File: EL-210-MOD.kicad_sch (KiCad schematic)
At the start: 29 parts, among them J1 Conn_01x05, J2 Conn_01x02, P1 EL-210-KEY, U1 9-ST-20, U2 STM32G0B1KET6, U3 MAX6934AQH+D, U4 TPS613221ADBV, U5 MAX4719EUB+, U6 TLV61046ADB

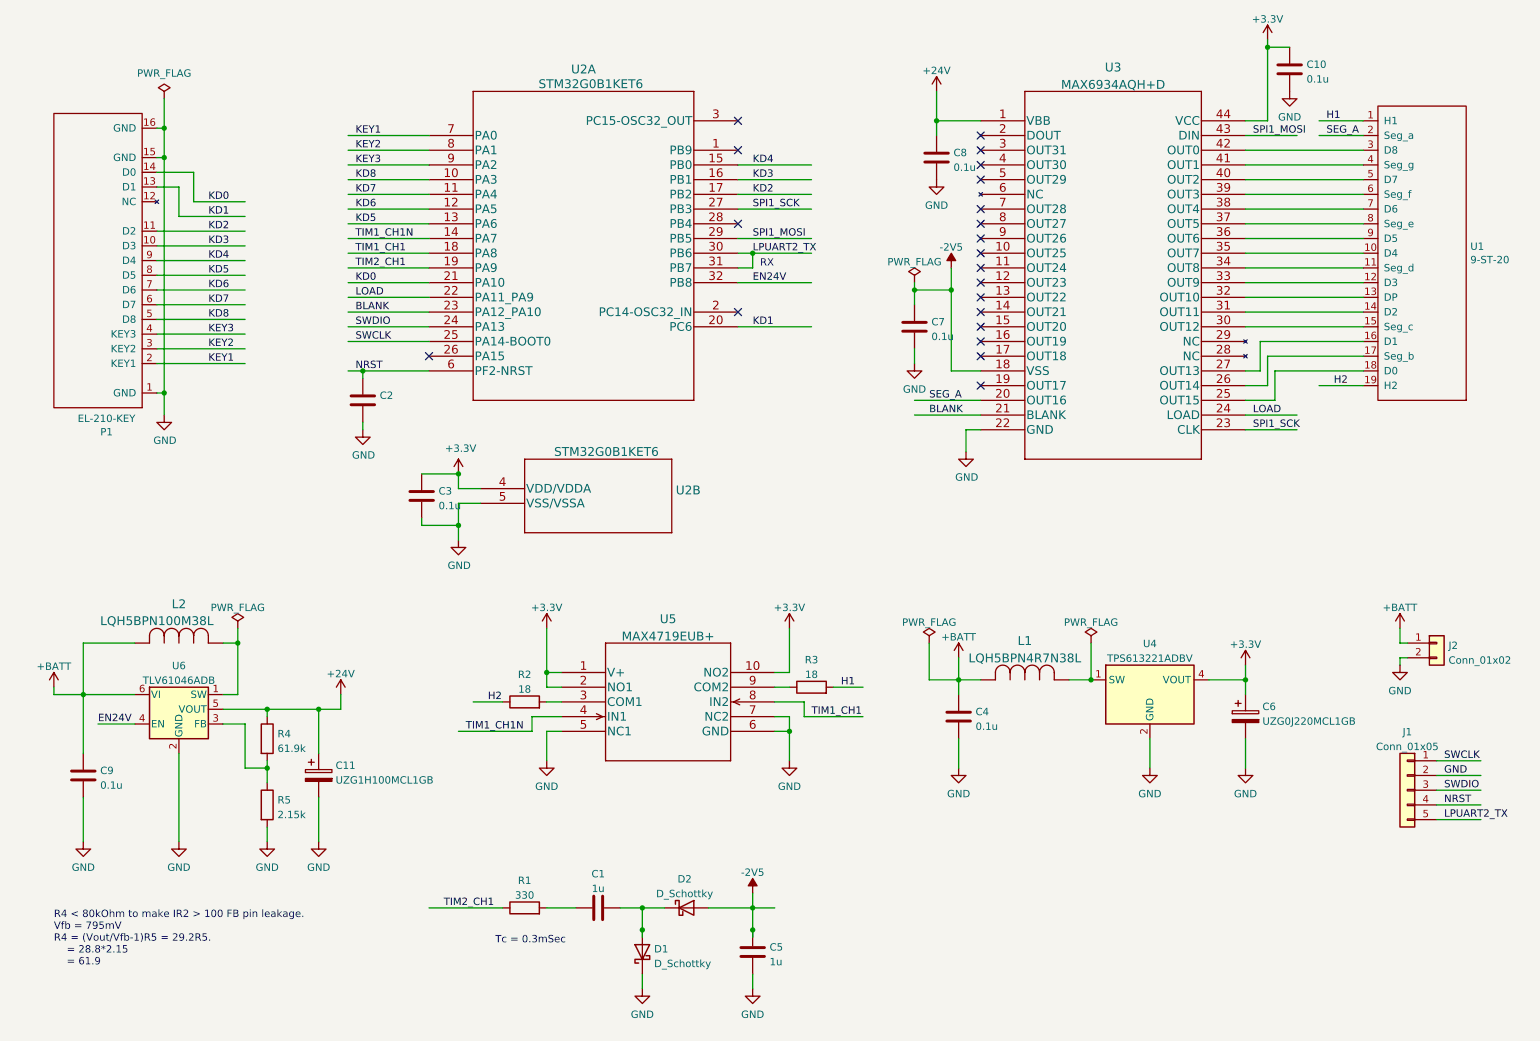
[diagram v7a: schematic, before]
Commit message: Layout finished.
DRC passed except silkscreen minor problem.
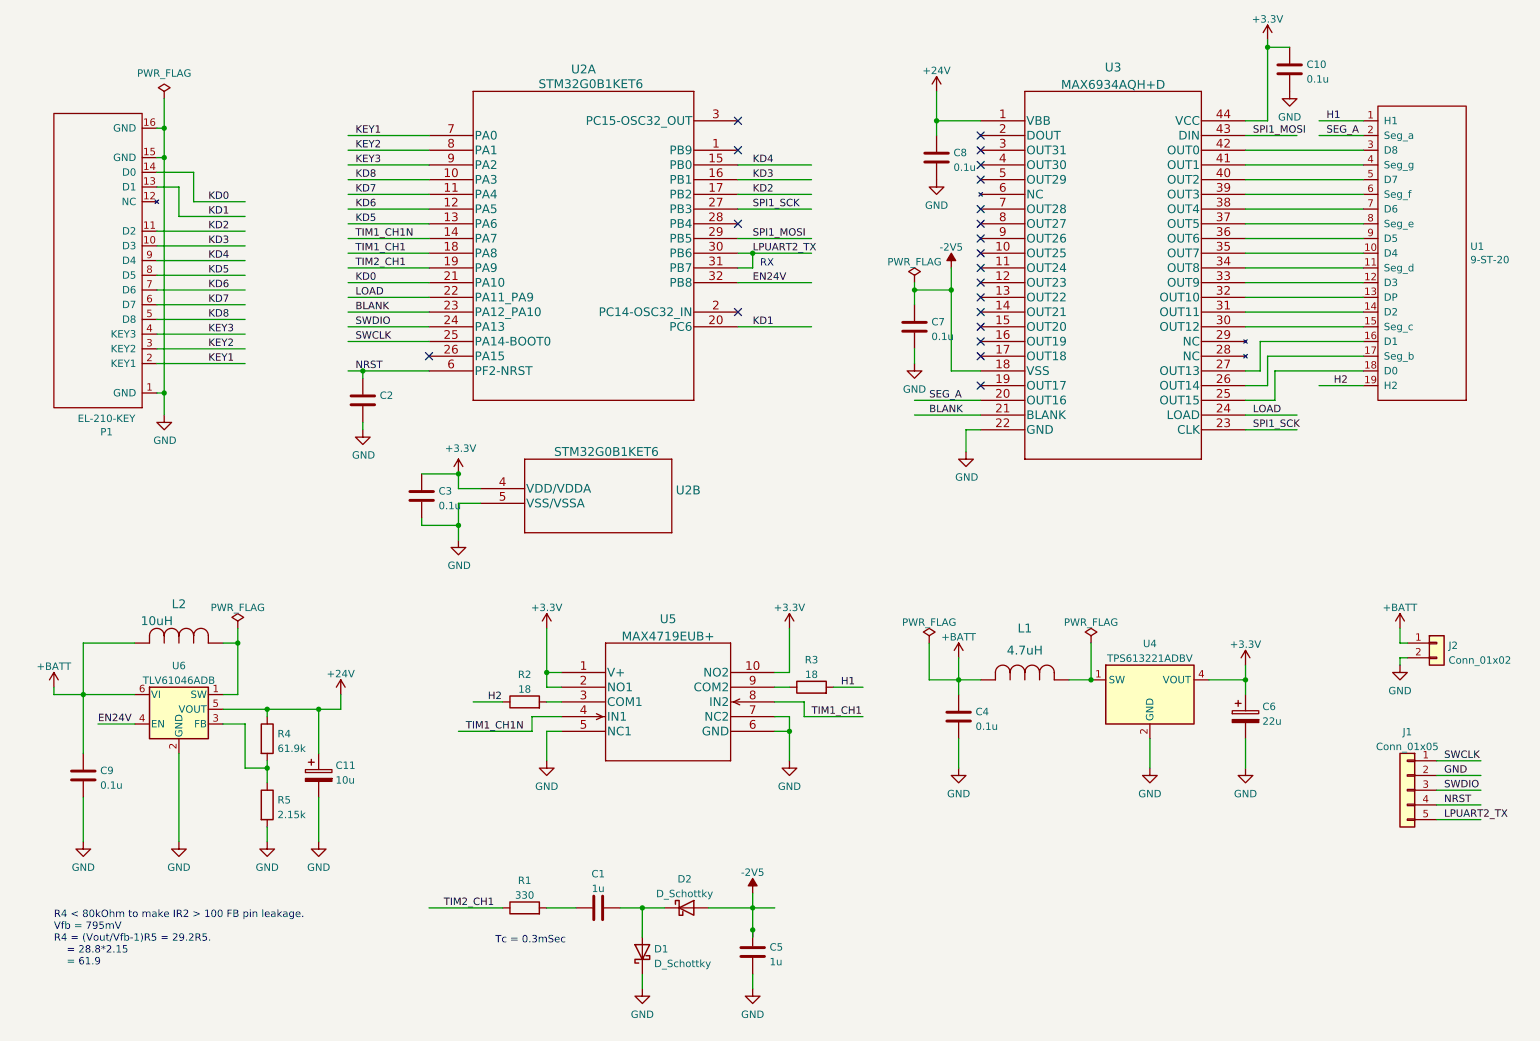
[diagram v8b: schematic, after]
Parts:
- C11: value UZG1H100MCL1GB -> 10u
- C6: value UZG0J220MCL1GB -> 22u
- L1: value LQH5BPN4R7N38L -> 4.7uH
- L2: value LQH5BPN100M38L -> 10uH
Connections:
- net at C1.2, D2.1 (K): no longer D1.2 (A)
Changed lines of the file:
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@@
   (junction (at 148.59 58.42) (diameter 0) (color 0 0 0 0)
-  )
-  (junction (at 129.54 175.26) (diameter 0) (color 0 0 0 0)
   )
   (junction (at 46.99 36.83) (diameter 0) (color 0 0 0 0)
@@
     (stroke (width 0) (type default) (color 0 0 0 0))
   )
-  (wire (pts (xy 129.54 171.45) (xy 129.54 175.26))
-    (stroke (width 0) (type default) (color 0 0 0 0))
-  )
   (wire (pts (xy 140.97 171.45) (xy 148.59 171.45))
     (stroke (width 0) (type default) (color 0 0 0 0))
@@
     (stroke (width 0) (type default) (color 0 0 0 0))
   )
-  (wire (pts (xy 129.54 175.26) (xy 129.54 176.53))
+  (wire (pts (xy 129.54 171.45) (xy 129.54 176.53))
     (stroke (width 0) (type default) (color 0 0 0 0))
   )
@@
       (effects (font (size 1.27 1.27)) hide)
     )
-    (property "Datasheet" "~" (id 3) (at 184.15 138.43 0)
+    (property "Datasheet" "1608M" (id 3) (at 184.15 138.43 0)
       (effects (font (size 1.27 1.27)) hide)
     )
@@
       (effects (font (size 1.27 1.27)) hide)
     )
-    (property "Datasheet" "~" (id 3) (at 121.92 171.45 0)
+    (property "Datasheet" "1608M" (id 3) (at 121.92 171.45 0)
       (effects (font (size 1.27 1.27)) hide)
     )
@@
       (effects (font (size 1.27 1.27)) hide)
     )
-    (property "Datasheet" "~" (id 3) (at 64.77 153.67 0)
+    (property "Datasheet" "1608M" (id 3) (at 64.77 153.67 0)
       (effects (font (size 1.27 1.27)) hide)
     )
@@
       (effects (font (size 1.27 1.27)) hide)
     )
-    (property "Datasheet" "~" (id 3) (at 109.22 171.45 0)
+    (property "Datasheet" "1608M" (id 3) (at 109.22 171.45 0)
       (effects (font (size 1.27 1.27)) hide)
     )
@@
       (effects (font (size 1.27 1.27)) (justify left))
     )
-    (property "Value" "UZG1H100MCL1GB" (id 1) (at 76.581 149.4032 0)
+    (property "Value" "10u" (id 1) (at 76.581 149.4032 0)
       (effects (font (size 1.27 1.27)) (justify left))
     )
@@
       (effects (font (size 1.27 1.27)) hide)
     )
-    (property "Datasheet" "~" (id 3) (at 73.66 148.59 0)
+    (property "Datasheet" "UZG1H100MCL1GB" (id 3) (at 73.66 148.59 0)
       (effects (font (size 1.27 1.27)) hide)
     )
@@
       (effects (font (size 1.27 1.27)) hide)
     )
-    (property "Datasheet" "~" (id 3) (at 81.28 83.82 0)
+    (property "Datasheet" "1608M" (id 3) (at 81.28 83.82 0)
       (effects (font (size 1.27 1.27)) hide)
     )
@@
       (effects (font (size 1.27 1.27)) hide)
     )
-    (property "Datasheet" "~" (id 3) (at 91.44 100.33 0)
+    (property "Datasheet" "1608M" (id 3) (at 91.44 100.33 0)
       (effects (font (size 1.27 1.27)) hide)
     )
@@
       (effects (font (size 1.27 1.27)) hide)
     )
-    (property "Datasheet" "~" (id 3) (at 137.16 171.45 0)
+    (property "Datasheet" "1608M" (id 3) (at 137.16 171.45 0)
       (effects (font (size 1.27 1.27)) hide)
     )
@@
       (effects (font (size 1.27 1.27)) hide)
     )
-    (property "Datasheet" "~" (id 3) (at 109.22 135.89 0)
+    (property "Datasheet" "1608M" (id 3) (at 109.22 135.89 0)
       (effects (font (size 1.27 1.27)) hide)
     )
@@
       (effects (font (size 1.27 1.27)) hide)
     )
-    (property "Datasheet" "~" (id 3) (at 33.02 148.59 0)
+    (property "Datasheet" "1608M" (id 3) (at 33.02 148.59 0)
       (effects (font (size 1.27 1.27)) hide)
     )
@@
       (effects (font (size 1.27 1.27)) hide)
     )
-    (property "Datasheet" "~" (id 3) (at 158.75 133.35 0)
+    (property "Datasheet" "1608M" (id 3) (at 158.75 133.35 0)
       (effects (font (size 1.27 1.27)) hide)
     )
@@
       (effects (font (size 1.27 1.27)) hide)
     )
-    (property "Datasheet" "~" (id 3) (at 129.54 179.07 0)
+    (property "Datasheet" "1608M" (id 3) (at 129.54 179.07 0)
       (effects (font (size 1.27 1.27)) hide)
     )
@@
       (effects (font (size 1.27 1.27)) hide)
     )
-    (property "Datasheet" "~" (id 3) (at 148.59 179.07 0)
+    (property "Datasheet" "1608M" (id 3) (at 148.59 179.07 0)
       (effects (font (size 1.27 1.27)) hide)
     )
@@
       (effects (font (size 1.27 1.27)) hide)
     )
-    (property "Datasheet" "~" (id 3) (at 241.3 26.67 0)
+    (property "Datasheet" "1608M" (id 3) (at 241.3 26.67 0)
       (effects (font (size 1.27 1.27)) hide)
     )
@@
       (effects (font (size 1.27 1.27)) hide)
     )
-    (property "Datasheet" "~" (id 3) (at 64.77 142.24 0)
+    (property "Datasheet" "1608M" (id 3) (at 64.77 142.24 0)
       (effects (font (size 1.27 1.27)) hide)
     )
@@
       (effects (font (size 1.27 1.27)) hide)
     )
-    (property "Datasheet" "~" (id 3) (at 180.34 41.91 0)
+    (property "Datasheet" "1608M" (id 3) (at 180.34 41.91 0)
       (effects (font (size 1.27 1.27)) hide)
     )
@@
       (effects (font (size 1.27 1.27)) (justify left))
     )
-    (property "Value" "UZG0J220MCL1GB" (id 1) (at 236.601 139.2432 0)
+    (property "Value" "22u" (id 1) (at 236.601 139.2432 0)
       (effects (font (size 1.27 1.27)) (justify left))
     )
@@
       (effects (font (size 1.27 1.27)) hide)
     )
-    (property "Datasheet" "~" (id 3) (at 233.68 138.43 0)
+    (property "Datasheet" "UZG0J220MCL1GB" (id 3) (at 233.68 138.43 0)
       (effects (font (size 1.27 1.27)) hide)
     )
@@
   (symbol (lib_id "LQH5BPN100M38L:LQH5BPN100M38L") (at 187.96 132.08 0) (unit 1)
     (in_bom yes) (on_board yes) (fields_autoplaced)
-    (property "Reference" "L1" (id 0) (at 195.58 125.3543 0)
+    (property "Reference" "L1" (id 0) (at 195.58 123.19 0)
       (effects (font (size 1.524 1.524)))
     )
-    (property "Value" "LQH5BPN4R7N38L" (id 1) (at 195.58 128.3477 0)
+    (property "Value" "4.7uH" (id 1) (at 195.58 127 0)
       (effects (font (size 1.524 1.524)))
     )
@@
       (effects (font (size 1.524 1.524)) hide)
     )
-    (property "Datasheet" "" (id 3) (at 187.96 132.08 0)
-      (effects (font (size 1.524 1.524)))
+    (property "Datasheet" "LQH5BPN4R7N38L" (id 3) (at 187.96 132.08 0)
+      (effects (font (size 1.524 1.524)) hide)
     )
     (pin "1")
@@
       (effects (font (size 1.524 1.524)))
     )
-    (property "Value" "LQH5BPN100M38L" (id 1) (at 45.72 121.92 0)
+    (property "Value" "10uH" (id 1) (at 45.72 121.92 0)
       (effects (font (size 1.524 1.524)))
     )
@@
       (effects (font (size 1.524 1.524)) hide)
     )
-    (property "Datasheet" "" (id 3) (at 41.91 125.73 0)
-      (effects (font (size 1.524 1.524)))
+    (property "Datasheet" "LQH5BPN100M38L" (id 3) (at 41.91 125.73 0)
+      (effects (font (size 1.524 1.524)) hide)
     )
     (pin "1")
@@
       (effects (font (size 1.27 1.27)) hide)
     )
-    (property "Datasheet" "~" (id 3) (at 176.53 71.12 0)
+    (property "Datasheet" "1608M" (id 3) (at 176.53 71.12 0)
       (effects (font (size 1.27 1.27)) hide)
     )
@@
     )
     (path "/c63c3bc3-bbbc-455a-8ec9-31c56f0d841f"
-      (reference "C6") (unit 1) (value "UZG0J220MCL1GB") (footprint "Capacitor_SMD:CP_Elec_6.3x3.9")
+      (reference "C6") (unit 1) (value "22u") (footprint "Capacitor_SMD:CP_Elec_6.3x3.9")
     )
     (path "/f5b00abc-a391-4427-9c9b-fa38c85349fd"
@@
     )
     (path "/2fdd038b-8927-431e-9c67-f8f1c25fc8d5"
-      (reference "C11") (unit 1) (value "UZG1H100MCL1GB") (footprint "Capacitor_SMD:CP_Elec_4x3.9")
+      (reference "C11") (unit 1) (value "10u") (footprint "Capacitor_SMD:CP_Elec_4x3.9")
     )
     (path "/9b4341eb-9497-42fa-9e5f-534332830100"
@@
     )
     (path "/c8ef8ae9-b11b-4ab4-b66d-011626d539e6"
-      (reference "L1") (unit 1) (value "LQH5BPN4R7N38L") (footprint "project_lib:LQH5BPN100M38L")
+      (reference "L1") (unit 1) (value "4.7uH") (footprint "project_lib:LQH5BPN100M38L")
     )
     (path "/ce10d06a-06bb-4ac3-b5cd-cc0d6cc0aabe"
-      (reference "L2") (unit 1) (value "LQH5BPN100M38L") (footprint "project_lib:LQH5BPN100M38L")
+      (reference "L2") (unit 1) (value "10uH") (footprint "project_lib:LQH5BPN100M38L")
     )
     (path "/00000000-0000-0000-0000-0000629f54c5"
